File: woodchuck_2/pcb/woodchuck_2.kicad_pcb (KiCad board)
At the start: 2 copper layers, 44 parts, among them IC1 Si4460, IC2 24AA01, IC3 ADP3335, IC4 MAX-7Q, P1 SWD, P2 COAX, P3 CONN_01X02, P4 COAX, U1 STM32F072CBT6, X1 Mounting hole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

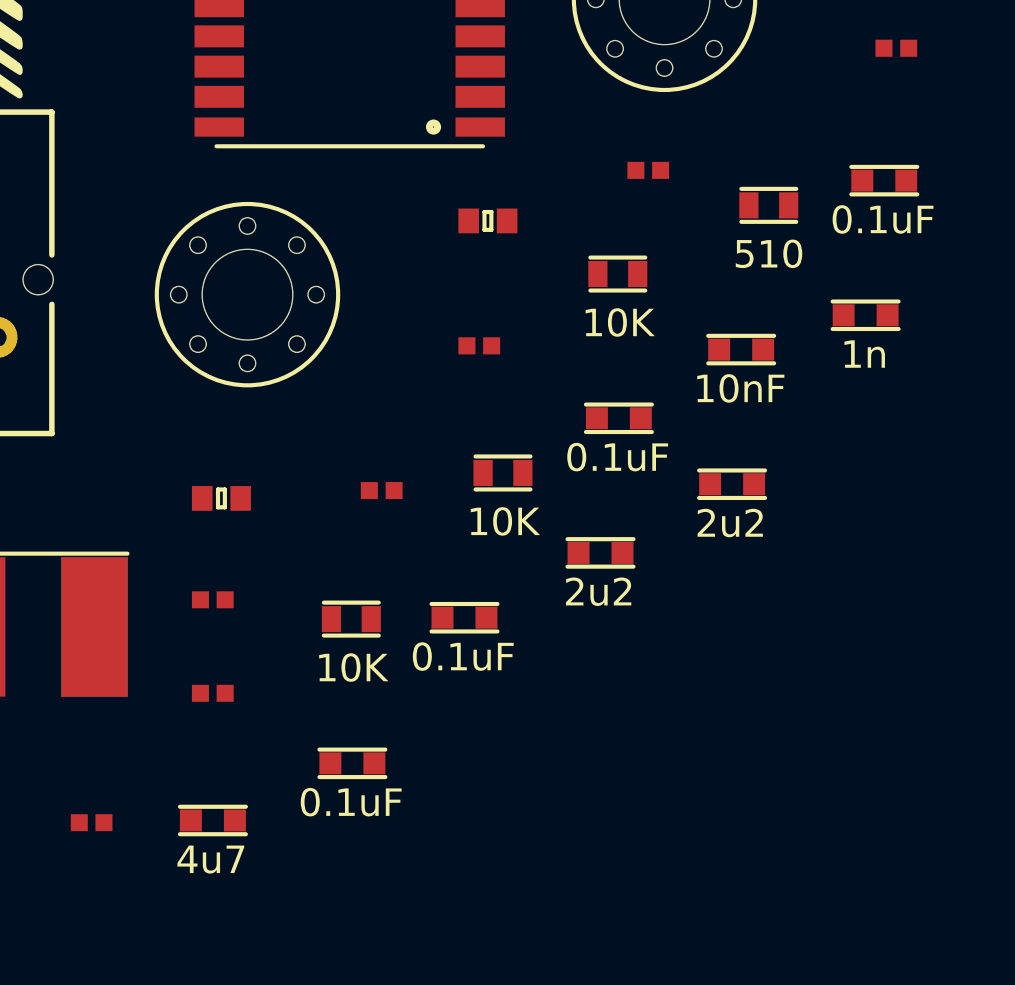
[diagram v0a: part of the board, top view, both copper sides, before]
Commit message: Change components to 0402, add farnell numbers and use different TCXO
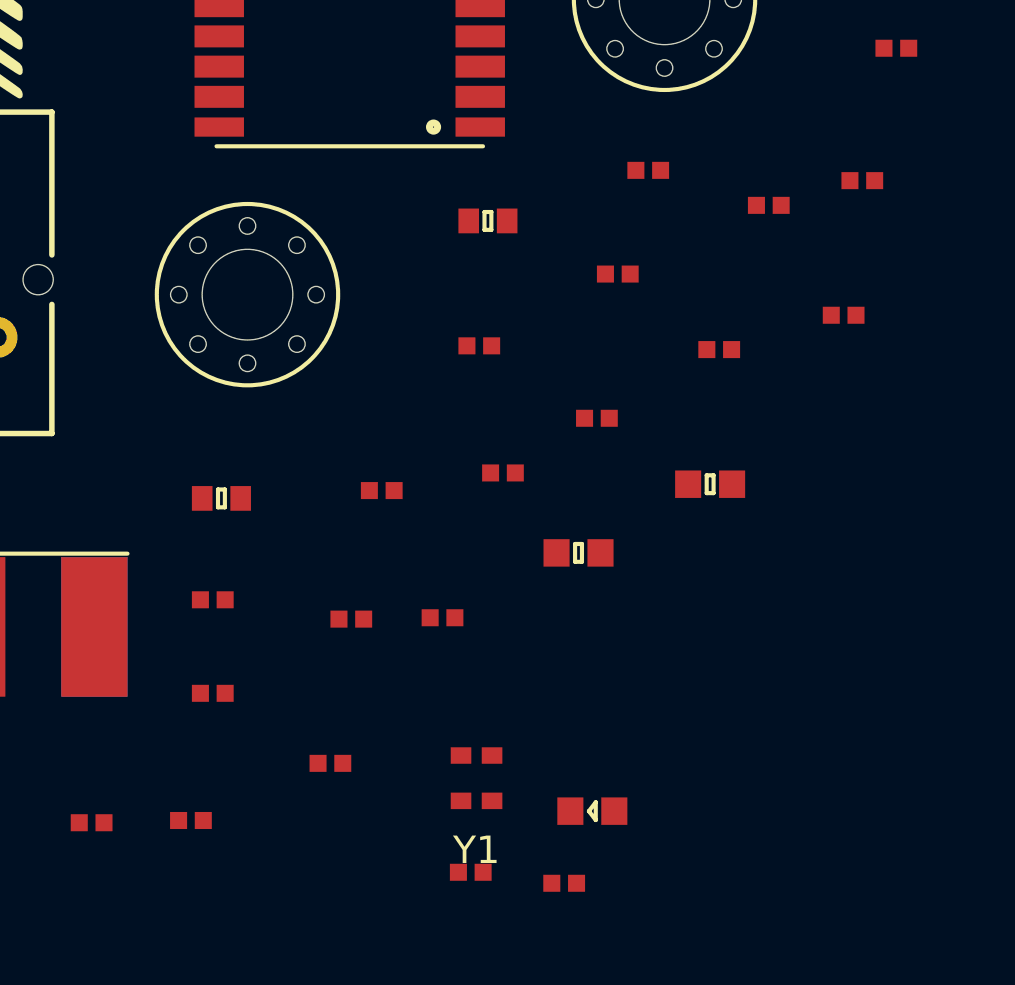
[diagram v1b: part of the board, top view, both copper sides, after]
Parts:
- added C21: 10nF, agg:0402, F.Cu at (168.4, 112.8)
- added C22: 100p, agg:0402, F.Cu at (171.8, 113.2)
- added D1: GRN_LED, agg:0603-LED, F.Cu at (172.9, 110.5)
- added Y1: TCXO, Woodchuck:TG-5006CJ, F.Cu at (168.7, 109.3)
- C16, C19, C2, C6, C7, C8, C9: footprint Woodchuck:C0603 -> agg:0402
- C17, C20: footprint Woodchuck:C0603 -> agg:0603
- L2: value LR1 -> 18nH
- R1, R2, R3, R4: footprint Woodchuck:0603 -> agg:0402
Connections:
- C20 pad 1: +3V3 -> GND
- C20 pad 2: GND -> +3V3
- IC1 pad 17: (no net) -> Net-(C22-Pad1)
- R1 pad 1: (no net) -> Net-(D1-Pad2)

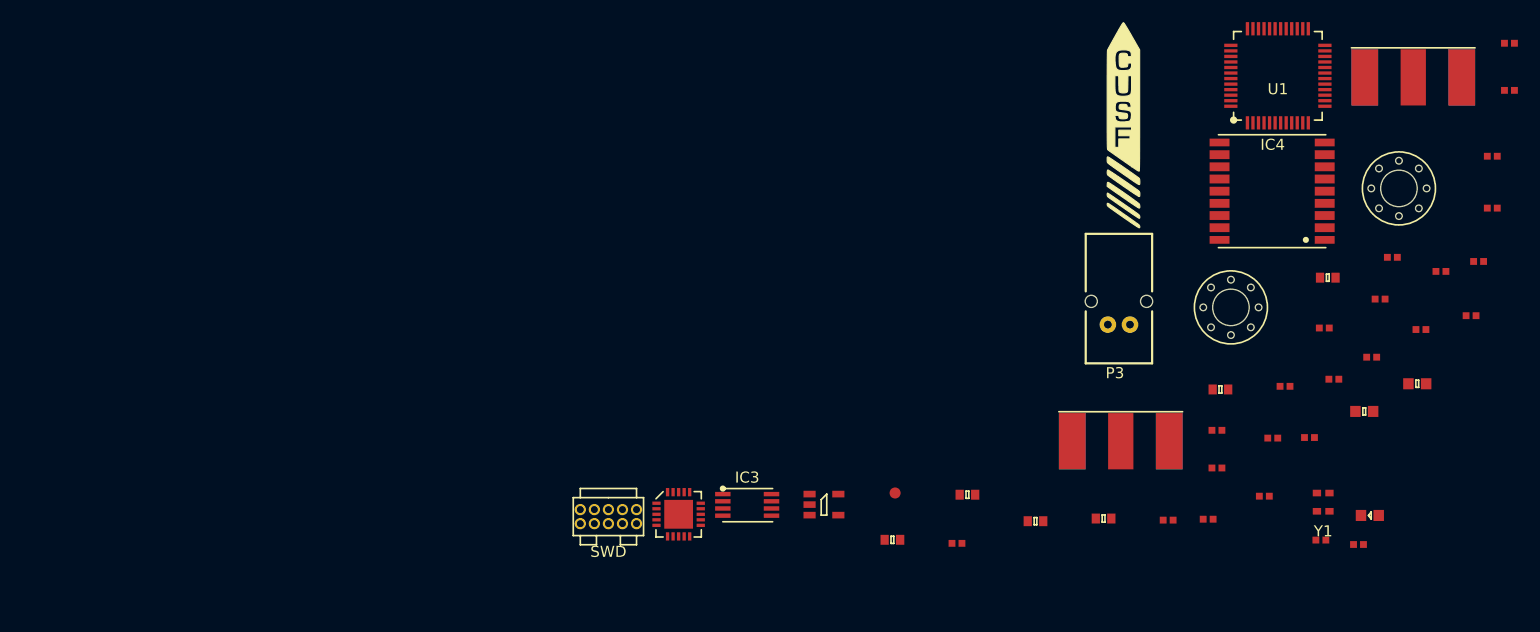
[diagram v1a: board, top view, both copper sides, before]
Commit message: Place components on board
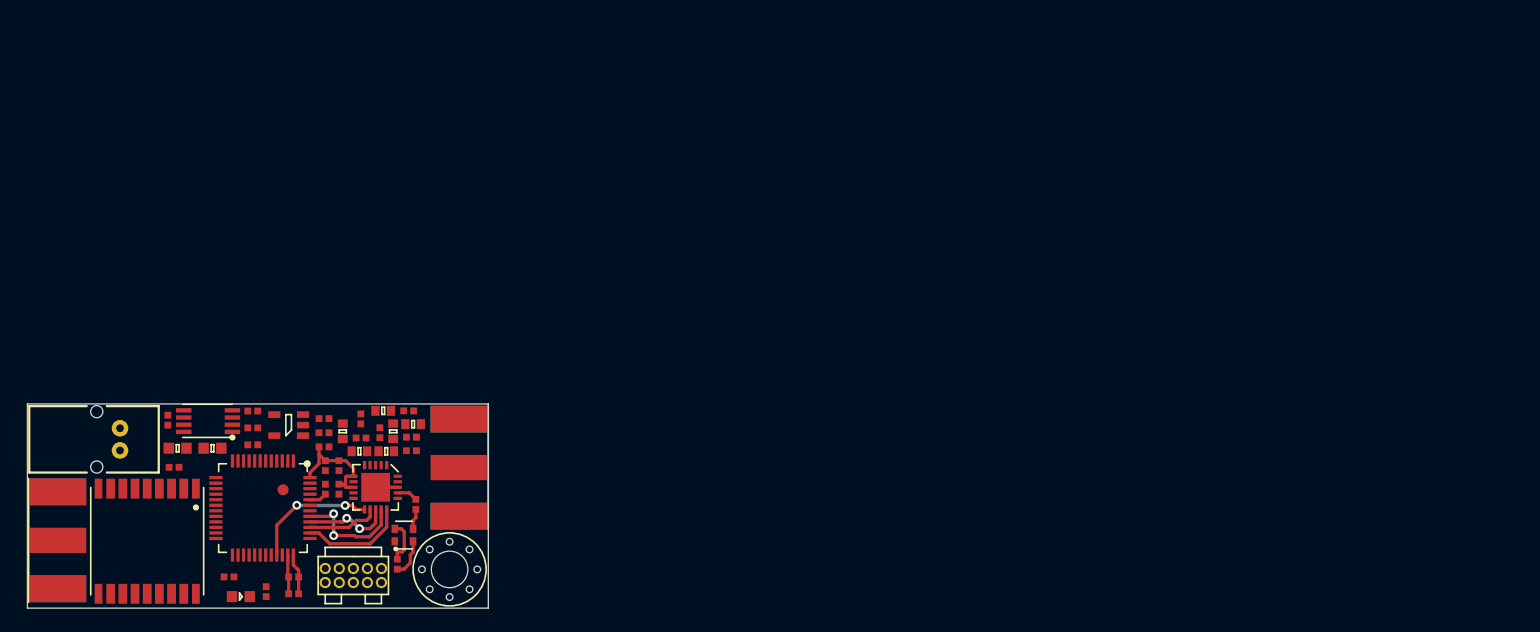
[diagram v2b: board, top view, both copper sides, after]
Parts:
- removed X3: CUSF LOGO, Woodchuck:cusf_logo
- removed X4: CUSF LOGO BACK, Woodchuck:cusf_logo_full
- X2: value Mounting hole -> CUSF LOGO BACK; footprint Woodchuck:M3_MOUNT -> Woodchuck:cusf_logo_small; moved to B.Cu
- moved C19 118.1 mm to (64.3, 101.9), turned to 90 degrees
- moved C1 112.2 mm to (78.5, 106.0), turned to 270 degrees
- moved R1 110.0 mm to (73.2, 117.4), turned to 90 degrees
- moved C11 109.7 mm to (81.7, 103.5)
- moved IC4 109.2 mm to (58.0, 117.6), turned to 90 degrees
- moved C20 109.0 mm to (68.3, 104.5)
- moved C17 107.3 mm to (65.2, 104.5), turned to 180 degrees
- moved C2 106.1 mm to (71.9, 104.1)
- moved C7 105.7 mm to (78.4, 104.3)
- moved C13 105.0 mm to (81.7, 101.8), turned to 90 degrees
- moved C12 102.5 mm to (83.4, 103.0), turned to 270 degrees
- moved D1 102.3 mm to (70.9, 117.9), turned to 180 degrees
- moved U1 99.7 mm to (72.9, 109.9), turned to 180 degrees
- moved C8 99.4 mm to (75.6, 116.1), turned to 180 degrees
- moved C6 98.4 mm to (69.8, 116.1), turned to 180 degrees
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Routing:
- net +3V3: track 0.00 -> 18.2 mm
- net /Radio_nIRQ: track 0.00 -> 11.6 mm, vias 0 -> 2
- net /Radio_SDI: track 0.00 -> 10.4 mm, vias 0 -> 2
- net /Radio_nSEL: track 0.00 -> 9.57 mm
- net GND: track 0.00 -> 8.60 mm
- net /Radio_SDO: track 0.00 -> 7.89 mm, vias 0 -> 2
- net /Radio_SCLK: track 0.00 -> 6.50 mm
- net Net-(C22-Pad1): track 0.00 -> 1.88 mm
- net Net-(C22-Pad2): track 0.00 -> 1.86 mm
- net Net-(R4-Pad2): track 0.00 -> 1.62 mm
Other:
- board outline added: 41.7 x 18.5 mm
- net class Default: clearance 0.2 -> 0.19; trace_width 0.25 -> 0.28; via_dia 0.6 -> 0.8
- net class Power added: clearance 0.19, trace_width 0.5, via_dia 0.8, via_drill 0.4
- rule trace_clearance: 0.2 -> 0.19
- rule trace_min: 0.2 -> 0.19
- rule via_min_size: 0.4 -> 0.8

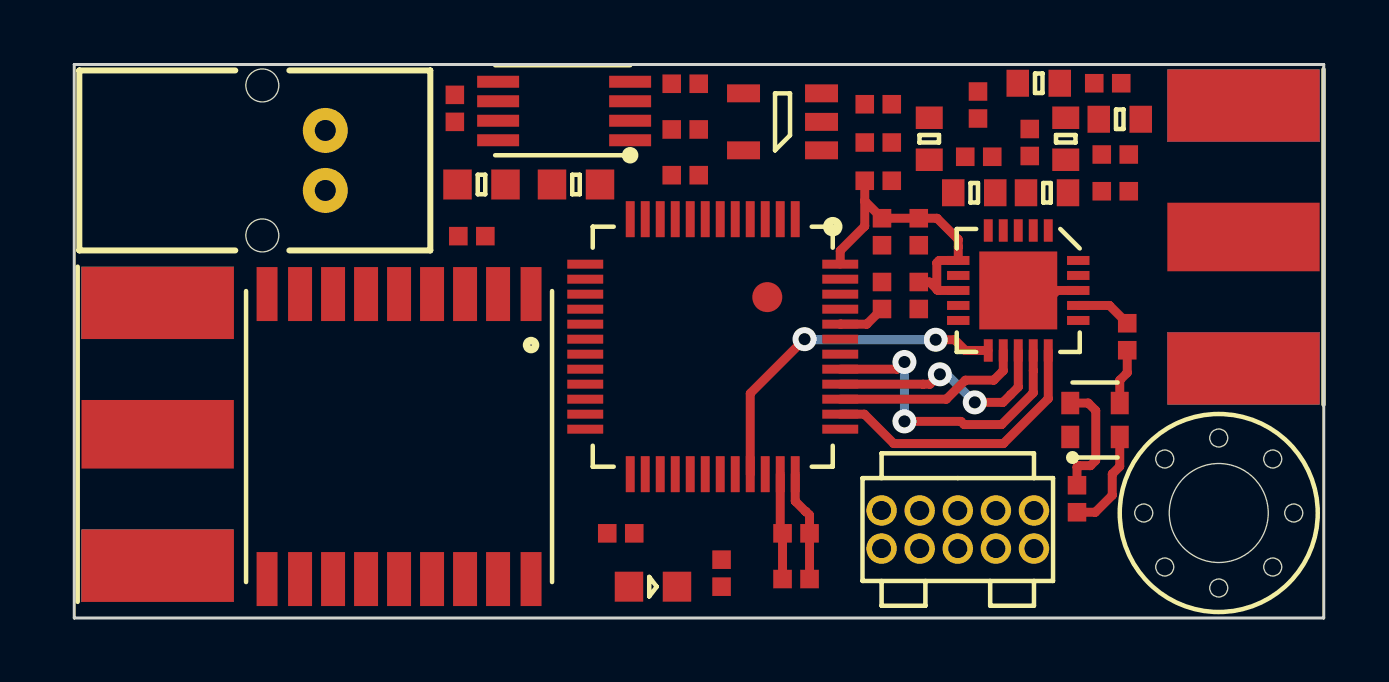
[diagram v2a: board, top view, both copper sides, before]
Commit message: Route Woodchuck 2
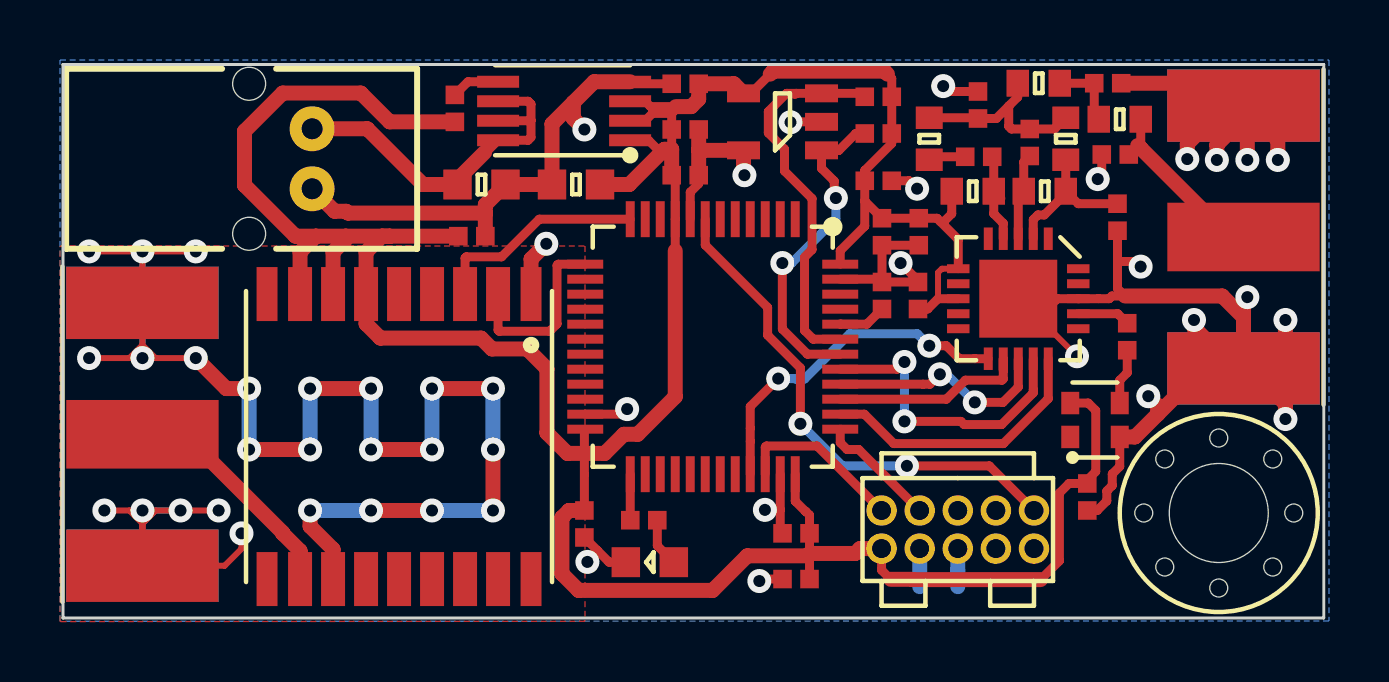
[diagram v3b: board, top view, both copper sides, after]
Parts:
- removed TP1: TESTPAD, agg:TESTPAD
- added X3: WOODCHUCK, Woodchuck:Woodchuck_2, B.Cu at (63.2, 109.0)
- moved R1 3.14 mm to (70.6, 115.6), turned to 0 degrees
- moved C6 1.25 mm to (68.6, 115.8), turned to 270 degrees
- moved X2 1.02 mm to (86.4, 106.8)
- moved C10 0.87 mm to (86.3, 105.5), turned to 270 degrees
- moved D1 0.82 mm to (70.8, 117.0), turned to 0 degrees
- moved P4 0.51 mm to (53.8, 112.8)
- moved P3 0.44 mm to (59.5, 104.6)
- moved C21 0.35 mm to (85.3, 114.9)
- moved R2 0.30 mm to (78.4, 102.8)
- moved IC1 0.28 mm to (83.0, 108.3)
- moved R3 0.25 mm to (78.4, 101.5)
- moved L2 0.09 mm to (83.9, 104.7)
- moved L1 0.07 mm to (81.5, 104.7)
- turned C5 to 90 degrees
- turned C16 to 180 degrees
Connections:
- R1 pad 1: Net-(D1-Pad2) -> Net-(R1-Pad1)
- R1 pad 2: Net-(R1-Pad2) -> Net-(D1-Pad2)
- U1 pad 16: Net-(R1-Pad2) -> (no net)
- U1 pad 25: (no net) -> Net-(R1-Pad1)
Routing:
- net GND: track 8.60 -> 150.1 mm, vias 0 -> 48
- net +3V3: track 18.2 -> 115.2 mm
- net /nRST: track 0.00 -> 17.1 mm, vias 0 -> 2
- net Net-(IC2-Pad3): track 0.00 -> 12.9 mm
- net +BATT: track 0.00 -> 12.2 mm
- net Net-(IC2-Pad1): track 0.00 -> 11.0 mm, vias 0 -> 2
- net Net-(IC4-Pad11): track 0.00 -> 10.7 mm
- net /TX_GPS_from_MCU: track 0.00 -> 7.24 mm
- net Net-(C12-Pad1): track 0.00 -> 6.48 mm
- net /RX_GPS_from_MCU: track 0.00 -> 6.19 mm
- net Net-(C15-Pad1): track 0.00 -> 6.13 mm
- net /SWDIO: track 0.00 -> 5.69 mm
- net Net-(C10-Pad1): track 0.00 -> 5.10 mm
- net /SWCLK: track 0.00 -> 4.03 mm
- net Net-(C11-Pad2): track 0.00 -> 3.15 mm
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- added copper zone on B.Cu, net GND
- added copper zone on F.Cu, net GND
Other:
- board size 41.7 x 18.5 mm -> 42 x 18.5 mm
- board text added: "16-03-2016"
- board text added: "G Brooks E R Eide A Raghu B Wong J M Wood"
- board text added: "Woodchuck 2"
- board text added: "www.cusf.co.uk"
